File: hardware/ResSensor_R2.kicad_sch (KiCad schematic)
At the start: 31 parts, among them J1 Conn_01x02, J2 Conn_01x04, U1 SPX3819M5-L-3-3, U2 STM32G030F6Px, U3 nRF24L01P, U4 CS1237, Y1 16MHz

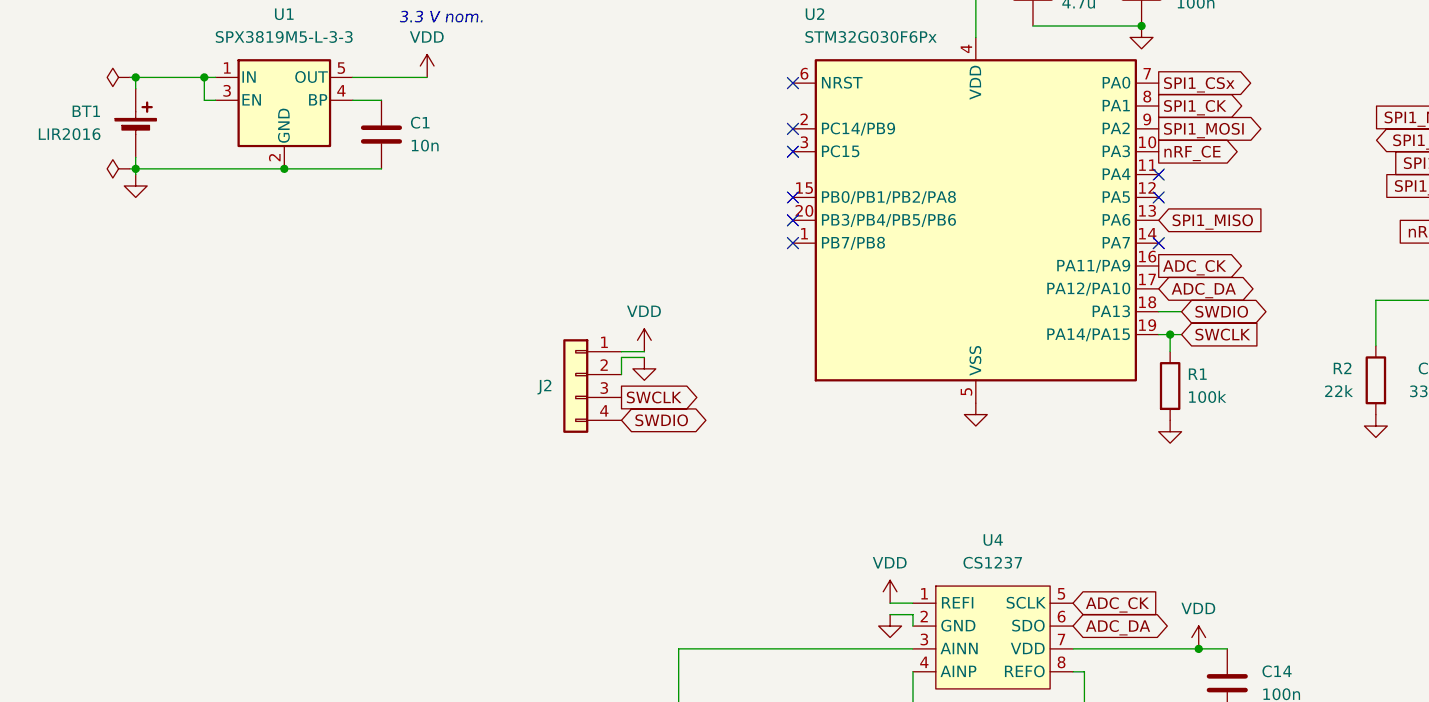
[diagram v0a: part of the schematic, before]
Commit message: Revise hardware, adding indicator LED
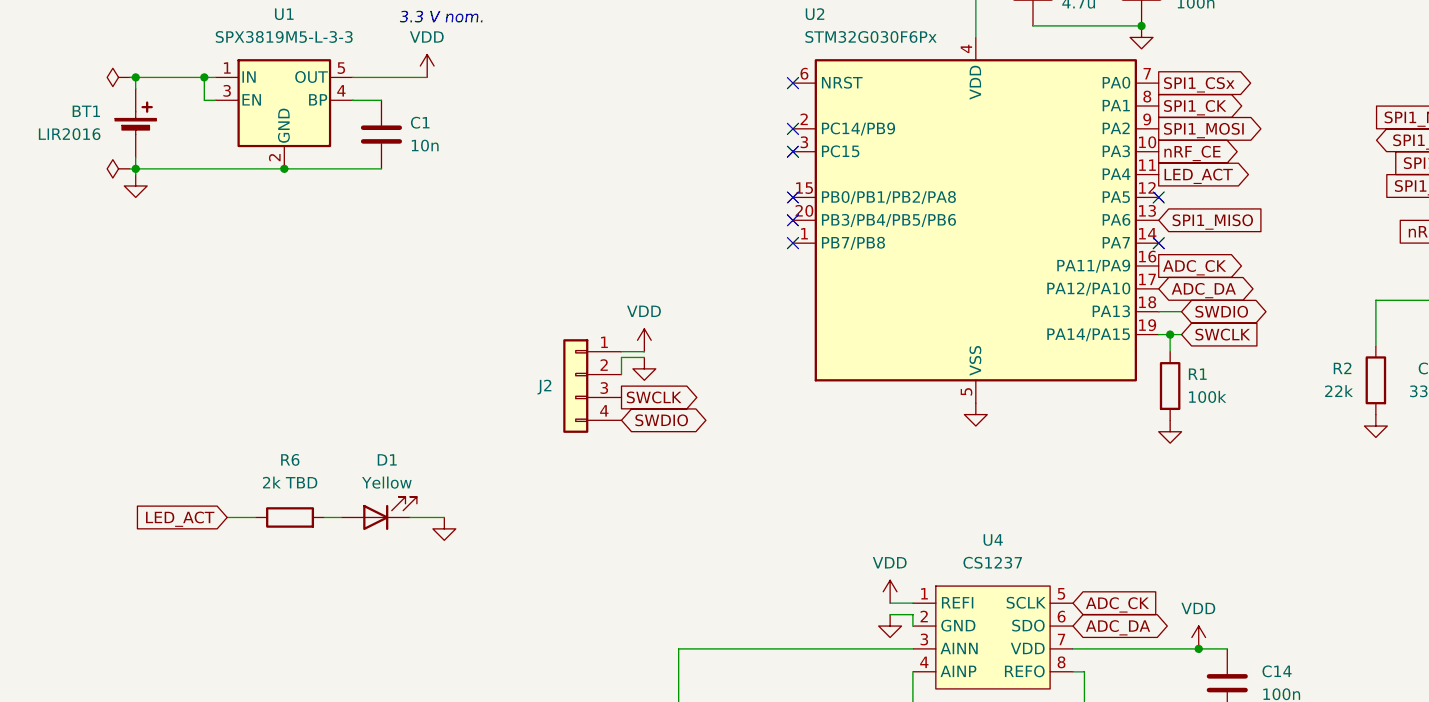
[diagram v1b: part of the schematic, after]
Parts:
- added D1: Yellow, LED_SMD:LED_0603_1608Metric, symbol Device:LED
- added R6: 2k TBD, Resistor_SMD:R_0603_1608Metric, symbol Device:R
- BT1: footprint Battery:BatteryHolder_Keystone_1060_1x2032 -> ResSensor_footprints:BatteryHolder_2032_THT_P20
- Y1: footprint Crystal:Crystal_SMD_3225-4Pin_3.2x2.5mm -> Crystal:Crystal_SMD_2016-4Pin_2.0x1.6mm
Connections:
- net GND: now also D1.1 (K)
- net LED_ACT: now reaches U2.11 (PA4)
- net LED_ACT: now also R6.1
- new net: D1.2 (A), R6.2
- no-connect marks 11 -> 10
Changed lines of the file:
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@@
   (no_connect (at 104.775 38.1))
   (no_connect (at 180.975 57.15))
-  (no_connect (at 145.415 48.26))
   (no_connect (at 104.775 53.34))
   (no_connect (at 259.08 58.42))
@@
   (no_connect (at 145.415 55.88))
   (no_connect (at 104.775 45.72))
+  (wire (pts (xy 52.705 86.36) (xy 54.61 86.36))
+    (stroke (width 0) (type default))
+  )
   (wire (pts (xy 110.49 109.22) (xy 110.49 113.665))
     (stroke (width 0) (type default))
@@
     (stroke (width 0) (type default))
   )
+  (wire (pts (xy 62.23 86.36) (xy 66.04 86.36))
+    (stroke (width 0) (type default))
+  )
   (wire (pts (xy 193.675 25.4) (xy 200.025 25.4))
     (stroke (width 0) (type default))
@@
   )
   (wire (pts (xy 31.75 47.625) (xy 31.75 48.26))
+    (stroke (width 0) (type default))
+  )
+  (wire (pts (xy 45.085 86.36) (xy 41.91 86.36))
     (stroke (width 0) (type default))
   )
@@
     )
   )
+  (global_label "LED_ACT" (shape output) (at 145.415 48.26 0) (fields_autoplaced)
+    (effects (font (size 1.27 1.27)) (justify left))
+    (property "Intersheetrefs" "${INTERSHEET_REFS}" (at 156.1411 48.26 0)
+      (effects (font (size 1.27 1.27)) (justify left) hide)
+    )
+  )
+  (global_label "LED_ACT" (shape input) (at 41.91 86.36 180) (fields_autoplaced)
+    (effects (font (size 1.27 1.27)) (justify right))
+    (property "Intersheetrefs" "${INTERSHEET_REFS}" (at 31.1839 86.36 0)
+      (effects (font (size 1.27 1.27)) (justify right) hide)
+    )
+  )
   (global_label "SPI1_MISO" (shape input) (at 145.415 53.34 0) (fields_autoplaced)
     (effects (font (size 1.27 1.27)) (justify left))
@@
       (effects (font (size 1.27 1.27)))
     )
-    (property "Footprint" "Crystal:Crystal_SMD_3225-4Pin_3.2x2.5mm" (at 221.615 64.77 0)
+    (property "Footprint" "Crystal:Crystal_SMD_2016-4Pin_2.0x1.6mm" (at 221.615 64.77 0)
       (effects (font (size 1.27 1.27)) hide)
     )
@@
       (effects (font (size 1.27 1.27)) (justify right))
     )
-    (property "Footprint" "Battery:BatteryHolder_Keystone_1060_1x2032" (at 31.75 42.291 90)
+    (property "Footprint" "ResSensor_footprints:BatteryHolder_2032_THT_P20" (at 31.75 42.291 90)
       (effects (font (size 1.27 1.27)) hide)
     )
@@
     )
   )
+  (symbol (lib_id "Device:R") (at 48.895 86.36 90) (unit 1)
+    (in_bom yes) (on_board yes) (dnp no) (fields_autoplaced)
+    (property "Reference" "R6" (at 48.895 80.01 90)
+      (effects (font (size 1.27 1.27)))
+    )
+    (property "Value" "2k TBD" (at 48.895 82.55 90)
+      (effects (font (size 1.27 1.27)))
+    )
+    (property "Footprint" "Resistor_SMD:R_0603_1608Metric" (at 48.895 88.138 90)
+      (effects (font (size 1.27 1.27)) hide)
+    )
+    (property "Datasheet" "~" (at 48.895 86.36 0)
+      (effects (font (size 1.27 1.27)) hide)
+    )
+    (pin "2")
+    (pin "1")
+    (instances
+      (project "ResSensor_R2"
+        (path "/4fdceb17-4902-4163-aeee-a94f9382439a"
+          (reference "R6") (unit 1)
+        )
+      )
+    )
+  )
   (symbol (lib_id "Device:C") (at 233.045 60.96 90) (unit 1)
     (in_bom yes) (on_board yes) (dnp no)
@@
     )
   )
+  (symbol (lib_id "power:GND") (at 66.04 86.36 0) (unit 1)
+    (in_bom yes) (on_board yes) (dnp no) (fields_autoplaced)
+    (property "Reference" "#PWR025" (at 66.04 92.71 0)
+      (effects (font (size 1.27 1.27)) hide)
+    )
+    (property "Value" "GND" (at 66.04 90.805 0)
+      (effects (font (size 1.27 1.27)) hide)
+    )
+    (property "Footprint" "" (at 66.04 86.36 0)
+      (effects (font (size 1.27 1.27)) hide)
+    )
+    (property "Datasheet" "" (at 66.04 86.36 0)
+      (effects (font (size 1.27 1.27)) hide)
+    )
+    (pin "1")
+    (instances
+      (project "ResSensor_R2"
+        (path "/4fdceb17-4902-4163-aeee-a94f9382439a"
+          (reference "#PWR025") (unit 1)
+        )
+      )
+    )
+  )
   (symbol (lib_id "Device:R") (at 146.685 71.755 0) (unit 1)
     (in_bom yes) (on_board yes) (dnp no) (fields_autoplaced)
@@
         )
       )
+    )
+  )
+  (symbol (lib_id "Device:LED") (at 58.42 86.36 180) (unit 1)
+    (in_bom yes) (on_board yes) (dnp no)
+    (property "Reference" "D1" (at 59.69 80.01 0)
+      (effects (font (size 1.27 1.27)))
+    )
+    (property "Value" "Yellow" (at 59.69 82.55 0)
+      (effects (font (size 1.27 1.27)))
+    )
+    (property "Footprint" "LED_SMD:LED_0603_1608Metric" (at 58.42 86.36 0)
+      (effects (font (size 1.27 1.27)) hide)
+    )
+    (property "Datasheet" "~" (at 58.42 86.36 0)
+      (effects (font (size 1.27 1.27)) hide)
+    )
+    (pin "1")
+    (pin "2")
+    (instances
+      (project "ResSensor_R2"
+        (path "/4fdceb17-4902-4163-aeee-a94f9382439a"
+          (reference "D1") (unit 1)
+        )
+      )

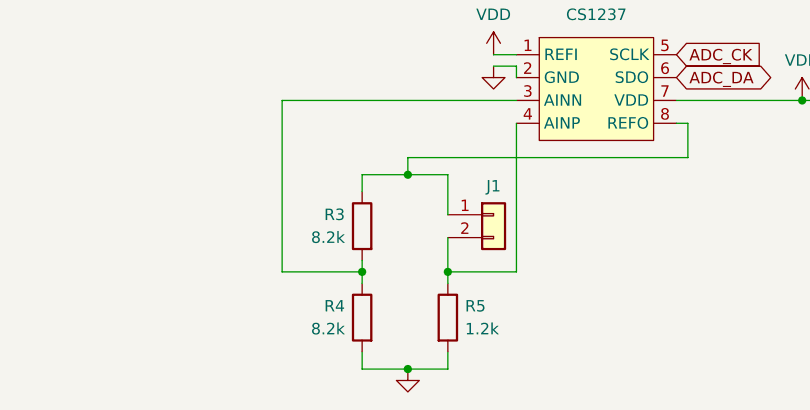
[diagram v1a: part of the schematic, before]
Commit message: Update firmware with blinking LED
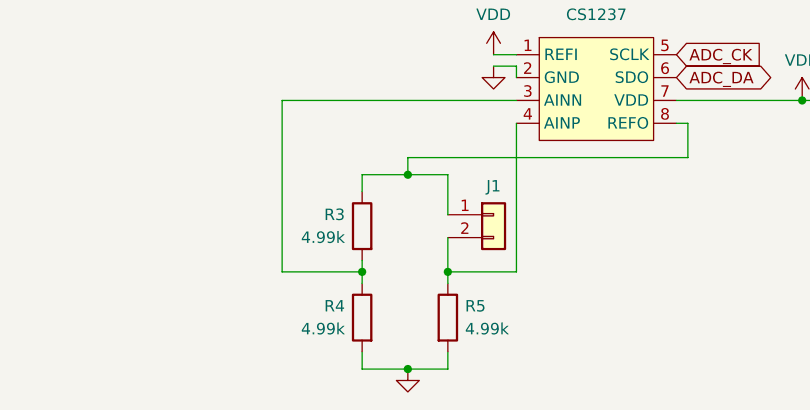
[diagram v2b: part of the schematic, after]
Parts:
- R3, R4: value 8.2k -> 4.99k
- R5: value 1.2k -> 4.99k
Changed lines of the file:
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@@
       (effects (font (size 1.27 1.27)) (justify left))
     )
-    (property "Value" "1.2k" (at 112.395 126.365 0)
+    (property "Value" "4.99k" (at 112.395 126.365 0)
       (effects (font (size 1.27 1.27)) (justify left))
     )
@@
       (effects (font (size 1.27 1.27)) (justify left))
     )
-    (property "Value" "8.2k" (at 99.06 116.205 0)
+    (property "Value" "4.99k" (at 99.06 116.205 0)
       (effects (font (size 1.27 1.27)) (justify left))
     )
@@
       (effects (font (size 1.27 1.27)) (justify left))
     )
-    (property "Value" "8.2k" (at 99.06 126.365 0)
-      (effects (font (size 1.27 1.27)) (justify left))
-    )
+    (property "Value" "4.99k" (at 99.06 126.365 0)
+      (effects (font (size 1.27 1.27)) (justify left))
+    )
